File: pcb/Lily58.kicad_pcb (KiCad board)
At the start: 2 copper layers, 142.5 x 106.3 mm, 74 parts, among them J1 LED, J2 5PIN, SW1 SW_PUSH, SW10 SW_PUSH, SW11 SW_PUSH, SW12 SW_PUSH, SW13 SW_PUSH, SW14 SW_PUSH, SW15 SW_PUSH, SW16 SW_PUSH, SW17 SW_PUSH, SW18 SW_PUSH, SW19 SW_PUSH, SW2 SW_PUSH, SW20 SW_PUSH, SW21 SW_PUSH, SW22 SW_PUSH, SW23 SW_PUSH, SW24 SW_PUSH, SW25 SW_PUSH, SW26 SW_PUSH, SW27 SW_PUSH, SW28 SW_PUSH, SW29 SW_PUSH, SW3 SW_PUSH, SW4 SW_PUSH, SW5 SW_PUSH, SW6 SW_PUSH, SW7 SW_PUSH, SW8 SW_PUSH, SW9 SW_PUSH, U1 ProMicro, U2 HOLE, U3 HOLE, U4 HOLE, U5 HOLE, U6 HOLE, U7 HOLE, U8 HOLE

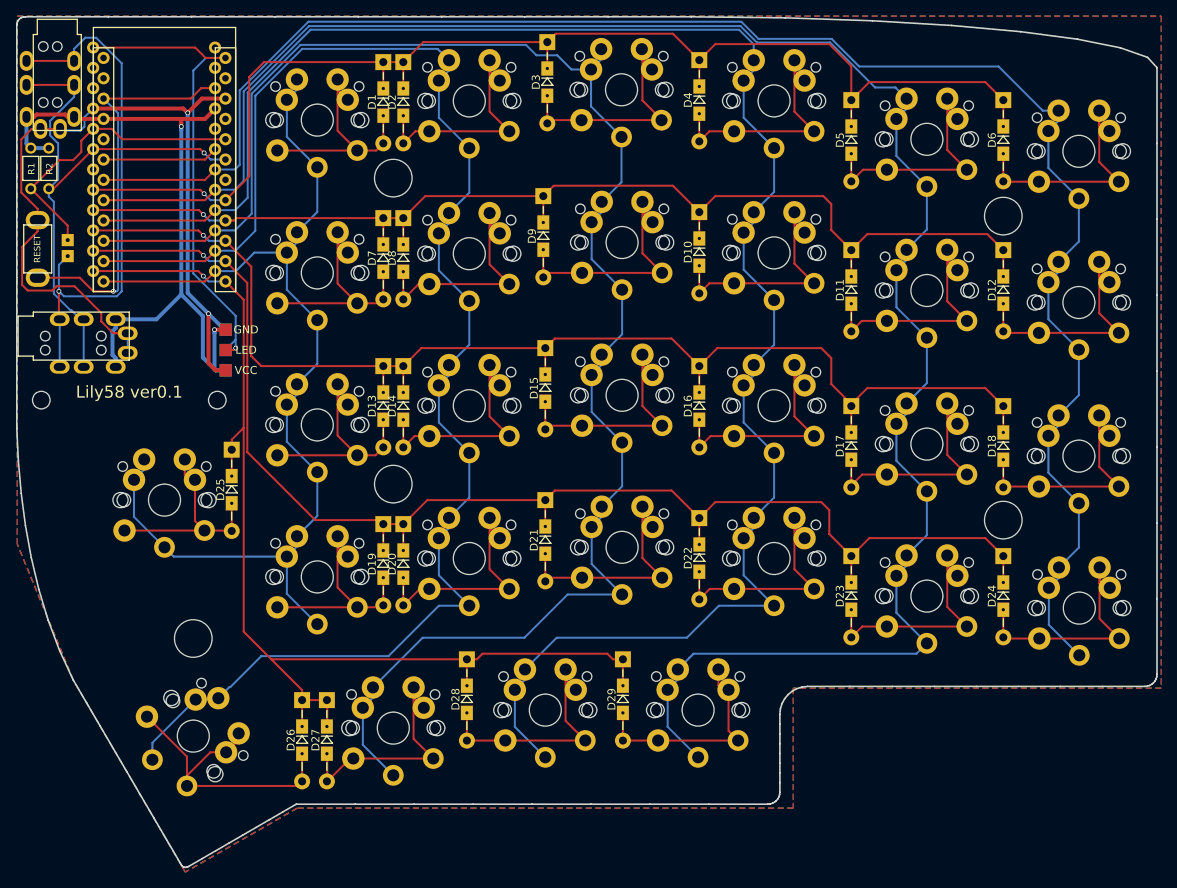
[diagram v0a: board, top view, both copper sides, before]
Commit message: update PCB 0.1->0.2
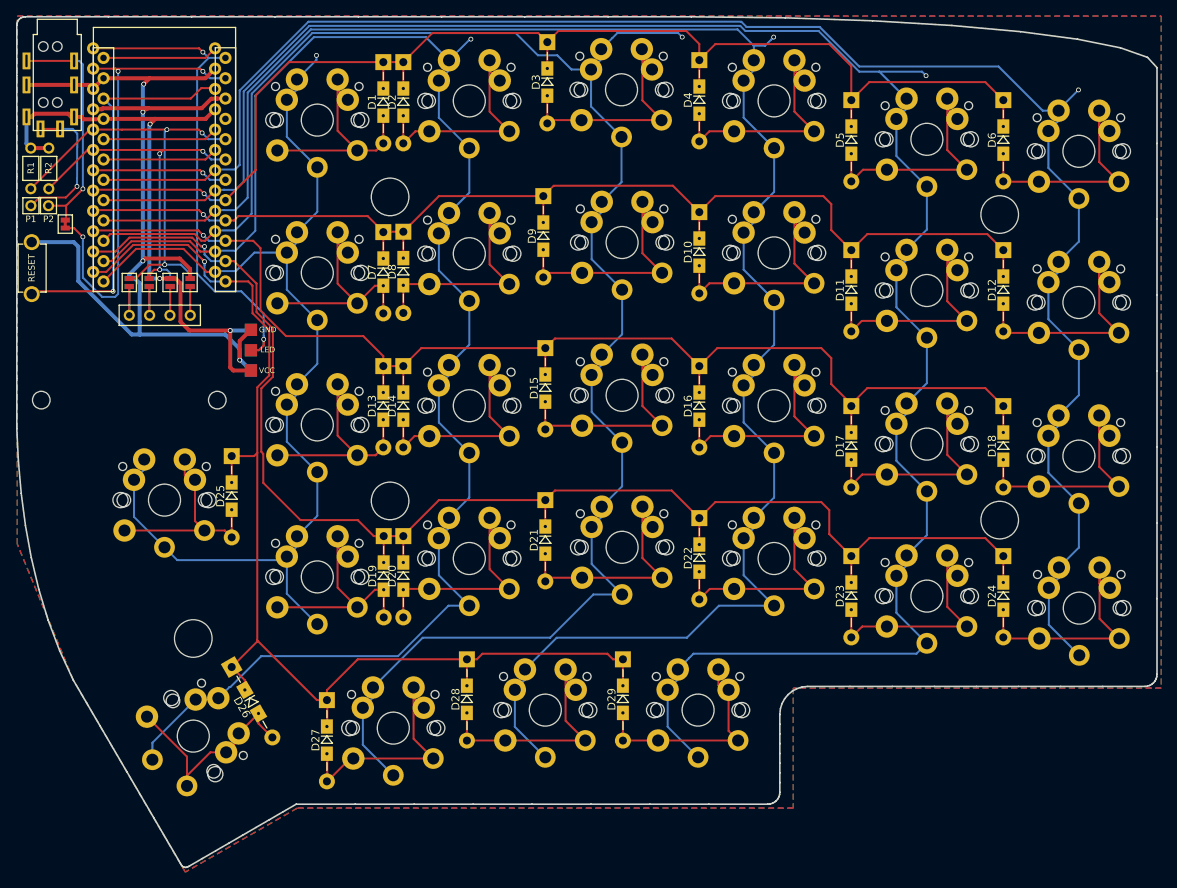
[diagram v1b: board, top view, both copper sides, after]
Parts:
- removed the J2 at (85.0, 77.0)
- removed the J2 at (88.0, 39.3)
- removed the U1 at (100.1, 54.9)
- removed the U1 at (101.4, 56.2)
- removed U2, U3: HOLE, Lily58-footprint:HOLE_M2
- removed U4, U5, U6, U7, U8: HOLE, Lily58-footprint:HOLE_M2_TH
- removed W1: jumper_smd, Lily58-footprint:jumper_smd_2dub
- added ?: Jumper_NO_Small, Lily58-footprint:Jumper, B.Cu at (97.0, 70.3)
- added ?: jumper, Lily58-footprint:jumper_data, F.Cu at (89.0, 63.0)
- added ?: OLED, Lily58-footprint:OLED_4Pin, F.Cu at (97.0, 74.4)
- added ?: Jumper_NO_Small, Lily58-footprint:Jumper, F.Cu at (104.6, 70.3)
- added ?: Jumper_NO_Small, Lily58-footprint:Jumper, F.Cu at (102.1, 70.3)
- added ?: Jumper_NO_Small, Lily58-footprint:Jumper, F.Cu at (99.5, 70.3)
- added ?: Jumper_NO_Small, Lily58-footprint:Jumper, F.Cu at (97.0, 70.3)
- added ?: Jumper_NO_Small, Lily58-footprint:Jumper, B.Cu at (104.6, 70.3)
- added ?: Jumper_NO_Small, Lily58-footprint:Jumper, B.Cu at (102.1, 70.3)
- added ?: Jumper_NO_Small, Lily58-footprint:Jumper, B.Cu at (99.5, 70.3)
- added G***: LOGO, Lily58-footprint:lily58_logo, B.Cu at (97.0, 82.0)
- added J2: 4PIN, Lily58-footprint:MJ-4PP-9, F.Cu at (88.0, 39.3)
- added P1: i2c_pin, Lily58-footprint:1pin_conn, F.Cu at (84.7, 60.7)
- added P2: i2c_pin, Lily58-footprint:1pin_conn, F.Cu at (86.9, 60.7)
- added TH1: HOLE, Lily58-footprint:HOLE_M2, F.Cu at (86.0, 85.0)
- added TH2: HOLE, Lily58-footprint:HOLE_M2, F.Cu at (108.0, 85.0)
- added TH3: HOLE, Lily58-footprint:HOLE_M2_TH, F.Cu at (129.6, 59.6)
- added TH4: HOLE, Lily58-footprint:HOLE_M2_TH, F.Cu at (205.8, 61.8)
- added TH5: HOLE, Lily58-footprint:HOLE_M2_TH, F.Cu at (129.6, 97.6)
- added TH6: HOLE, Lily58-footprint:HOLE_M2_TH, F.Cu at (205.8, 100.0)
- added TH7: HOLE, Lily58-footprint:HOLE_M2_TH, F.Cu at (105.0, 114.8)
- added U1: ProMicro, Lily58-footprint:ProMicro_rev2, F.Cu at (101.3, 55.8)
- ?: renamed from RSW1; value SW_PUSH -> SW_RST
- moved D26 7.92 mm to (112.3, 122.7), turned to 300 degrees
- moved J1 3.15 mm to (112.2, 81.3)
- moved ? 2.60 mm to (84.8, 68.5)
- moved D7 1.75 mm to (128.8, 69.0)
- moved D8 1.70 mm to (131.3, 69.0)
- moved D19 1.50 mm to (128.8, 107.0)
- moved D20 1.50 mm to (131.2, 107.0)
- moved D25 0.80 mm to (109.8, 97.0)
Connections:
- J1 pad 1: GND -> VCC
- J1 pad 3: VCC -> GND
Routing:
- net /xtradata: track 66.5 -> 0.00 mm, vias 1 -> 0
- net DATA: track 0.00 -> 58.9 mm, vias 0 -> 3
- net Net-(J2-Pad3): track 0.00 -> 29.8 mm, vias 0 -> 1
- net SCL: track 70.1 -> 43.9 mm, vias 1 -> 3
- net GND: track 105.9 -> 126.4 mm, vias 2 -> 4
- net Net-(J2-Pad4): track 0.00 -> 18.2 mm, vias 0 -> 1
- net SDA: track 37.1 -> 54.5 mm, vias 0 -> 3
- net Net-(U1-Pad7): track 0.00 -> 17.0 mm, vias 0 -> 1
- net (no net): track 14.5 -> 0.00 mm
- net Net-(U1-Pad24): track 0.00 -> 14.4 mm
- net Net-(U1-Pad20): track 0.00 -> 14.4 mm
- net Net-(U1-Pad19): track 0.00 -> 14.4 mm
- net col3: track 210.4 -> 223.6 mm, vias 0 -> 1
- net VCC: track 87.7 -> 76.8 mm, vias 2 -> 3
- net Net-(D26-Pad2): track 37.9 -> 27.0 mm
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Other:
- net class GND added: clearance 0.2, trace_width 0.5, via_dia 0.6, via_drill 0.4
- board text added: "GND"
- board text added: "LED"
- board text added: "VCC"
- board text added: "Ver 0.2 Beta"
- board text removed: "Lily58 ver0.1"

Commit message: fix PCB
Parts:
- removed ?: SW_RST, Lily58-footprint:TACT_SWITCH_TVBP06
- removed ? (x8): Jumper_NO_Small, Lily58-footprint:Jumper
- removed ?: jumper, Lily58-footprint:jumper_data
- removed ?: OLED, Lily58-footprint:OLED_4Pin
- added P3: ICSP, Lily58-footprint:ICSP, F.Cu at (105.0, 76.3)
- added RSW1: SW_RST, Lily58-footprint:TACT_SWITCH_TVBP06, F.Cu at (85.1, 68.5)
- added W1: jumper, Lily58-footprint:jumper_data, F.Cu at (89.0, 60.7)
- moved U1 0.32 mm to (101.0, 55.9)
- moved D9 0.25 mm to (149.0, 64.5)
- moved G*** 0.22 mm to (97.2, 82.1)
- moved J2 0.10 mm to (87.9, 39.3)
- moved SW3 0.07 mm to (158.6, 46.2)
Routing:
- net SDA: track 54.5 -> 27.5 mm, vias 3 -> 1
- net SCL: track 43.9 -> 24.2 mm, vias 3 -> 1
- net RESET: track 49.5 -> 65.5 mm, vias 1 -> 2
- net col2: track 232.4 -> 245.9 mm
- net Net-(J3-Pad2): track 7.23 -> 0.00 mm
- net Net-(J3-Pad4): track 7.22 -> 0.00 mm
- net Net-(J3-Pad3): track 7.22 -> 0.00 mm
- net Net-(J3-Pad1): track 7.20 -> 0.00 mm
- net col5: track 140.2 -> 134.2 mm, vias 1 -> 0
- net col1: track 251.6 -> 245.7 mm, vias 1 -> 0
- net GND: track 126.4 -> 122.4 mm, vias 4 -> 3
- net col4: track 199.7 -> 203.4 mm
- net col0: track 221.3 -> 217.9 mm, vias 1 -> 0
- net Net-(J2-Pad4): track 18.2 -> 14.8 mm
- net row4: track 147.3 -> 144.6 mm
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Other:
- board text added: "PCB Design by @F_YUUCHI"
- board text added: "Ver Beta"
- board text removed: "Ver 0.2 Beta"

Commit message: Lily58 PCBData update
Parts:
- added G***: LOGO, Lily58-footprint:lily58_logo_2, F.Cu at (97.0, 81.2)
- added G***: LOGO, Lily58-footprint:lily58_logo_3, B.Cu at (100.6, 55.0)
- added G***: LOGO, Lily58-footprint:lily58_logo_3, F.Cu at (100.5, 55.0)
- added JP1: , Lily58-footprint:Jumper, F.Cu at (104.3, 70.4)
- added JP2: , Lily58-footprint:Jumper, F.Cu at (101.8, 70.4)
- added JP3: , Lily58-footprint:Jumper, F.Cu at (99.2, 70.4)
- added JP4: , Lily58-footprint:Jumper, F.Cu at (96.7, 70.4)
- added JP5: , Lily58-footprint:Jumper, B.Cu at (104.3, 70.4)
- added JP6: , Lily58-footprint:Jumper, B.Cu at (101.8, 70.4)
- added JP7: , Lily58-footprint:Jumper, B.Cu at (99.2, 70.4)
- added JP8: , Lily58-footprint:Jumper, B.Cu at (96.7, 70.4)
- added OLED: OLED, Lily58-footprint:MY_SIL-4, F.Cu at (96.7, 75.0)
- G***: footprint Lily58-footprint:lily58_logo -> Lily58-footprint:lily58_logo_2
- TH1, TH2: footprint Lily58-footprint:HOLE_M2 -> Lily58-footprint:M2_HOLE_PCB
- moved P3 14.0 mm to (91.0, 75.0)
- moved G*** 0.92 mm to (97.0, 81.2)
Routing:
- net SDA: track 27.5 -> 53.7 mm, vias 1 -> 3
- net SCL: track 24.2 -> 42.8 mm, vias 1 -> 3
- net VCC: track 77.7 -> 94.8 mm, vias 2 -> 3
- net Net-(JP3-Pad1): track 0.00 -> 8.23 mm
- net Net-(JP2-Pad1): track 0.00 -> 8.22 mm
- net Net-(JP1-Pad1): track 0.00 -> 8.22 mm
- net Net-(JP4-Pad1): track 0.00 -> 8.20 mm
- net RESET: track 65.5 -> 57.5 mm, vias 2 -> 1
- net GND: track 122.4 -> 117.4 mm, vias 3 -> 4
- net col3: track 225.6 -> 229.7 mm, vias 1 -> 0
- net col5: track 134.2 -> 135.9 mm
- net Net-(J2-Pad3): track 28.2 -> 26.7 mm
- net col4: track 203.4 -> 204.8 mm, vias 1 -> 0
- net row4: track 144.6 -> 145.9 mm
- net col2: track 245.9 -> 246.8 mm
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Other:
- outline, holes or cut-outs redrawn
- board text added: "PCB Design by F_YUUCHI"
- board text removed: "PCB Design by @F_YUUCHI"
- board text removed: "Ver Beta"
